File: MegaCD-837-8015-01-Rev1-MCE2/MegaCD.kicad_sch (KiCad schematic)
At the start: 132 parts, among them CN1 CON 25P ANGLE, CN2 EDGE 60P, CN3 CON 21P, IC1 68HC000, IC10 MB8464A-10L, IC11 TC511664BZ, IC12 TC511664BZ, IC13 TC51832, IC14 TC51832, IC15 LC8951, IC16 74HC86, IC17 MB8464A-90L, IC18 MB8464A-90L, IC19 74AC74, IC2 315-5548, IC20 74HC245, IC3 315-5476A, IC4 27C1024, IC5 MB81C4256Z, IC5678 HM514270, IC6 MB81C4256Z, IC7 MB81C4256Z, IC8 MB81C4256Z, IC9 MB3790, J2 2TS, J3 MH, J4 CAS0, M0 TestPoint, M1 TestPoint, M10 TestPoint, M11 TestPoint, M192 TestPoint, M2 TestPoint, M3 TestPoint, M4 TestPoint, M5 TestPoint, M57 TestPoint, M6 TestPoint, M7 TestPoint, M8 TestPoint, M9 TestPoint

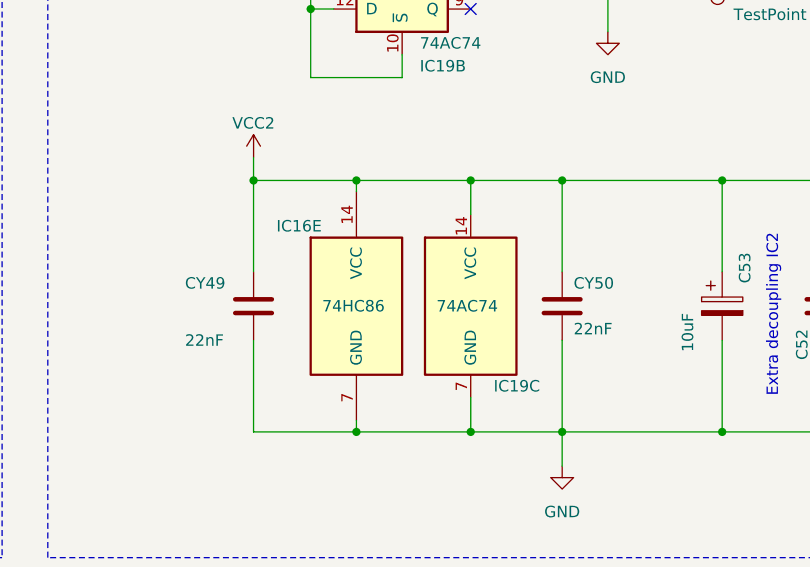
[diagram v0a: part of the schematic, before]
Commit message: Add 837-8952 Export board, minor updates for Japanese revisions (#1)
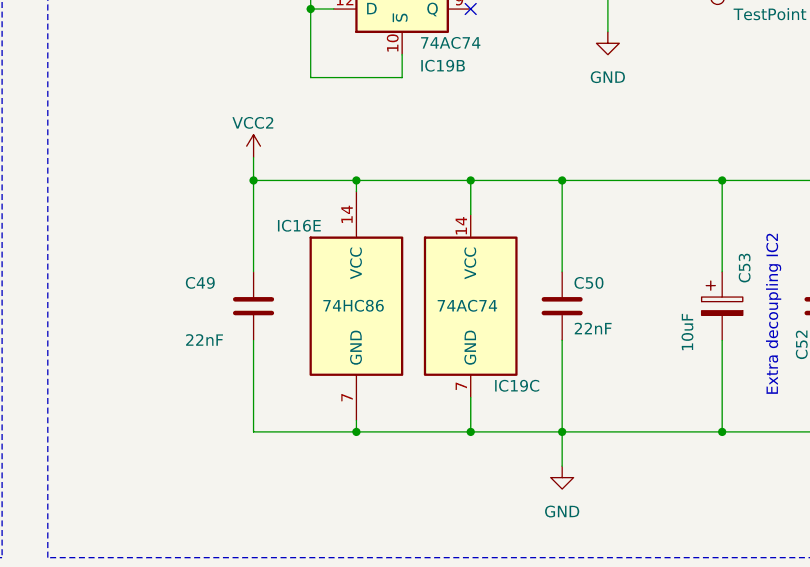
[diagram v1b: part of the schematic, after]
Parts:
- C1, C14, C15, C16, C17, C18, C2, C20, C21, C22, C24, C25, C27, C29, C3, C30, C32, C33, C34, C35, C36, C38, C39, C4, C40, C43, C44, C45, C47, C5, C51, C52, C54, C55, C56, C5678, C57, C58, C6, C7, C8, CT1, CX49, CX50, J1, J2, J3, J4, J5, R1, R2, R3, R4, R5, R6, R7: footprint MegaCD_Footprints:SMD_0805_HandSolder -> MegaCD_Footprints:SMD_0805_HandSolder_Medium
- C19: footprint MegaCD_Footprints:SMD_0805_HandSolder -> MegaCD_Footprints:SMD_0805_HandSolder_Narrow
- C49: renamed from CY49; footprint MegaCD_Footprints:SMD_0805_HandSolder -> MegaCD_Footprints:SMD_0805_HandSolder_Medium; now in the parts list
- C50: renamed from CY50; footprint MegaCD_Footprints:SMD_0805_HandSolder -> MegaCD_Footprints:SMD_0805_HandSolder_Medium; now in the parts list
